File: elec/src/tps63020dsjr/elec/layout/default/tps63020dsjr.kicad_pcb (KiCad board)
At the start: 2 copper layers, 225.7 x 100.8 mm, 10 parts

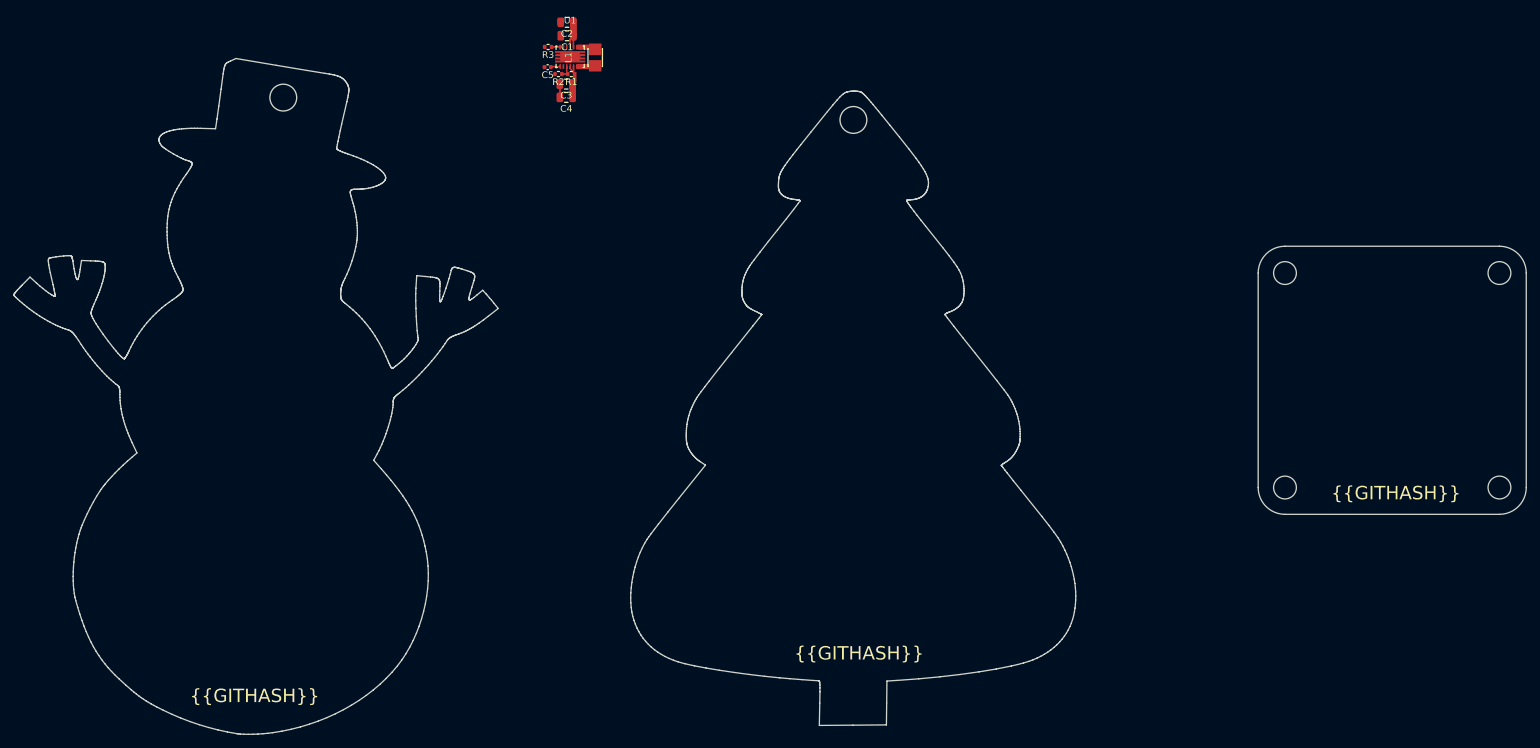
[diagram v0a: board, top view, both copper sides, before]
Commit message: Add layout for base
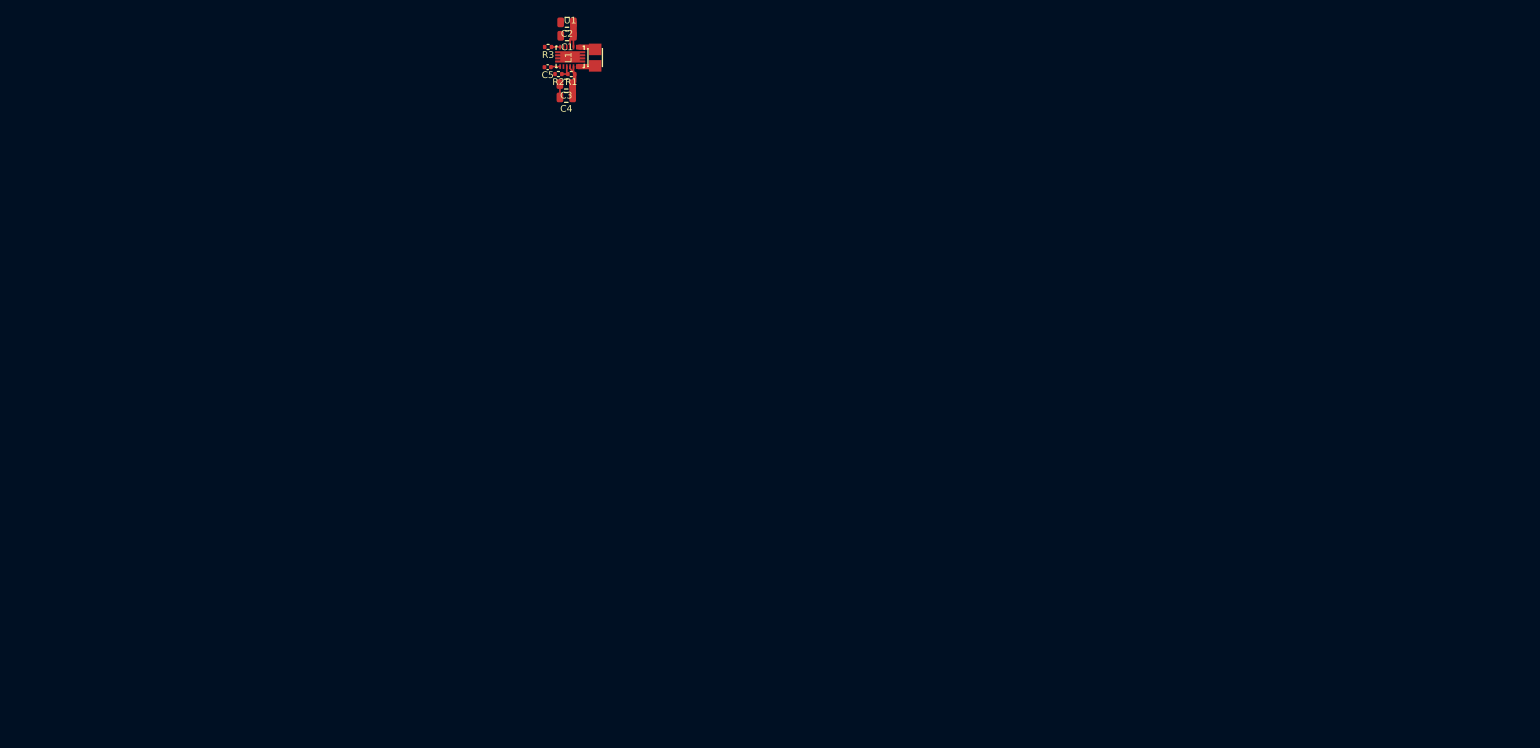
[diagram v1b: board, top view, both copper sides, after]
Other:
- board outline removed
- board text removed: "{{GITHASH}}"
